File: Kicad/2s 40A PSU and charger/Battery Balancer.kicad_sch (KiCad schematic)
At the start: 18 parts, among them J1 JST XH-S, Q6 Vishay sir404dp, U1 BQ76905RGRR

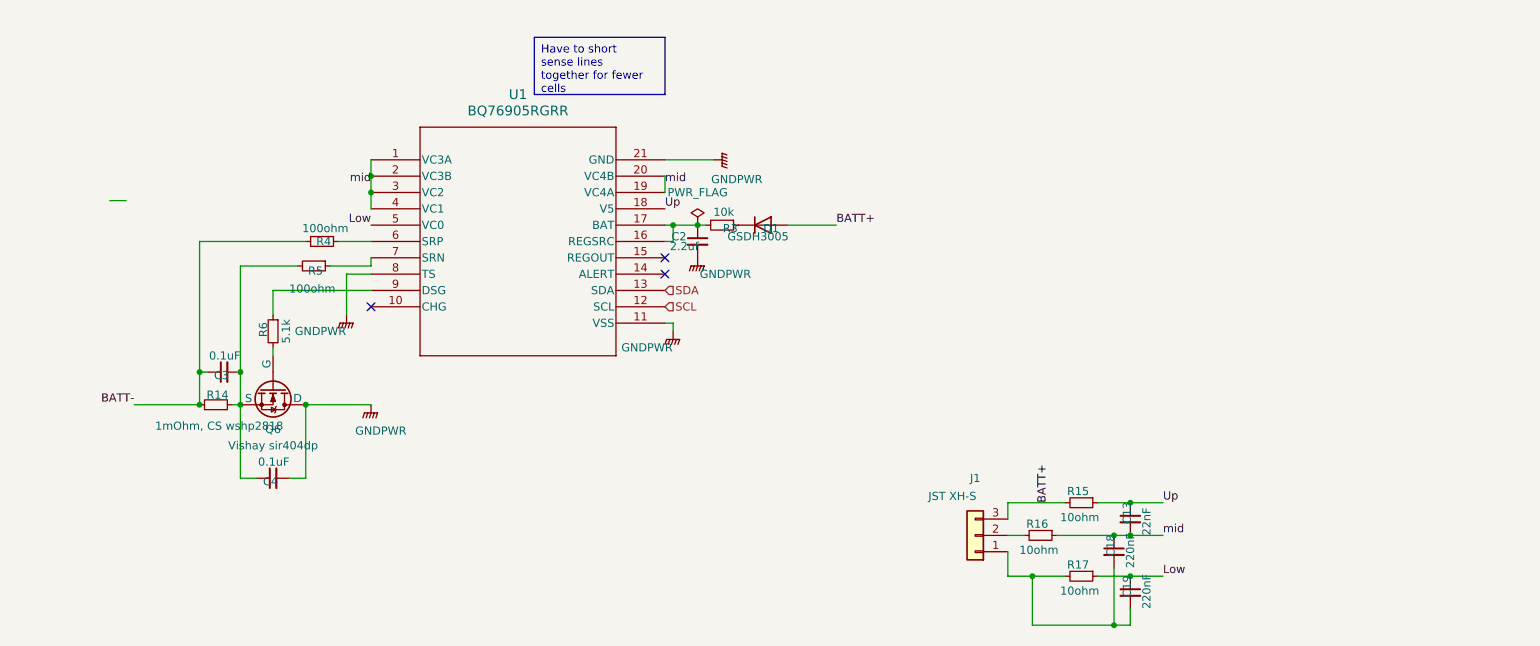
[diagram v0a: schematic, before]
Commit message: Reworked PSU to use CH32X035 and USB-PD
This will save a few bucks and will actually be a cooler solution than just a DC jack connected to some pads
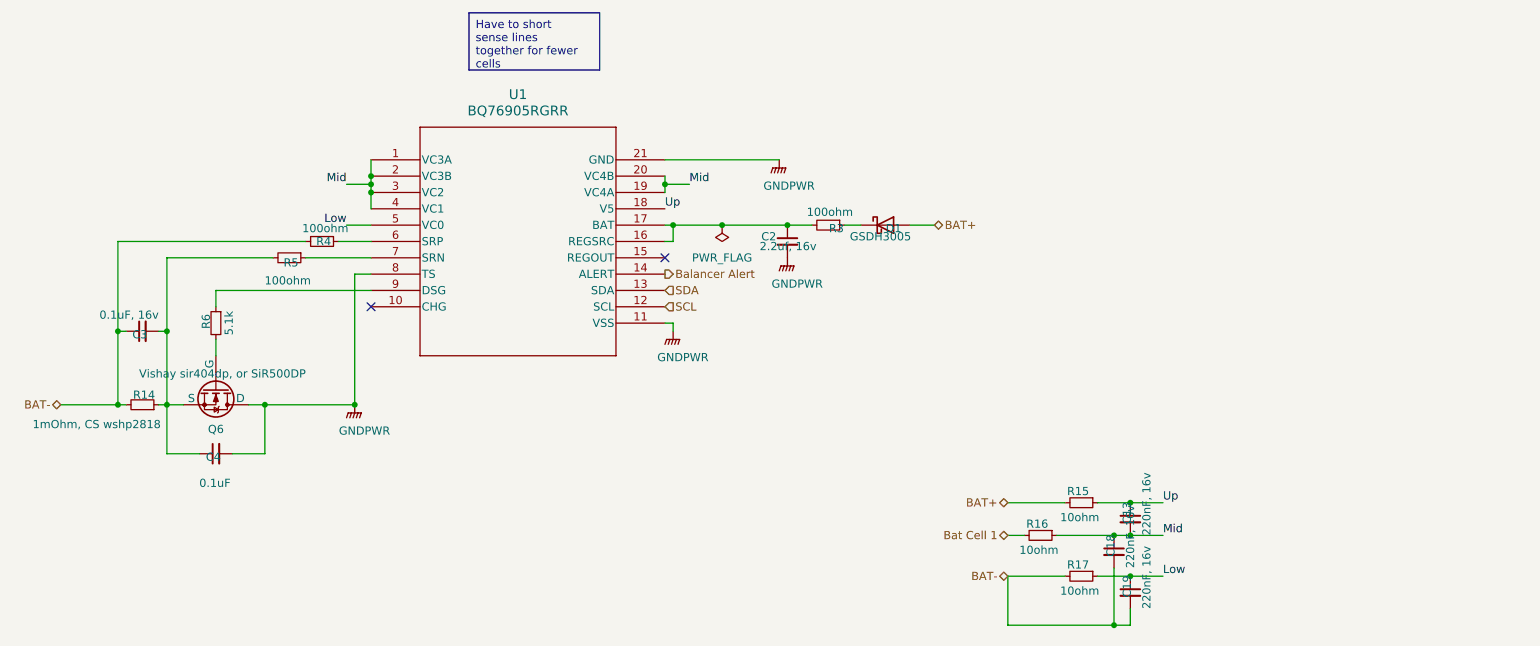
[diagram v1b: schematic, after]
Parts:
- removed J1: JST XH-S, Connector_JST:JST_XH_S3B-XH-A_1x03_P2.50mm_Horizontal, symbol Connector_Generic:Conn_01x03
- C13: value 22nF -> 220nF, 16v; footprint Capacitor_SMD:C_0603_1608Metric -> Capacitor_SMD:C_0402_1005Metric
- C18, C19: value 220nF -> 220nF, 16v; footprint Capacitor_SMD:C_0603_1608Metric -> Capacitor_SMD:C_0402_1005Metric
- C2: value 2.2uf -> 2.2uf, 16v
- C3: value 0.1uF -> 0.1uF, 16v; footprint Capacitor_SMD:C_0603_1608Metric -> Capacitor_SMD:C_0402_1005Metric
- C4: footprint Capacitor_SMD:C_0603_1608Metric -> Capacitor_SMD:C_0402_1005Metric
- D1: symbol Device:D -> Device:D_Schottky
- Q6: value Vishay sir404dp -> Vishay sir404dp, or SiR500DP
- R15, R16, R17, R4, R5, R6: footprint Resistor_SMD:R_0603_1608Metric -> Resistor_SMD:R_0402_1005Metric
- R3: value 10k -> 100ohm; footprint Resistor_SMD:R_0603_1608Metric -> Resistor_SMD:R_0402_1005Metric
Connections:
- net BATT- is gone; now on net BAT-: C3.1, R14.2, R4.2
- net Balancer Alert: now reaches U1.14 (ALERT)
- net Bat Cell 1: now reaches R16.2
- net BAT-: now reaches C18.2, C19.2, R17.2
- net BATT+ renamed BAT+
- net mid renamed Mid
- no-connect marks 3 -> 2
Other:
- moved on the sheet: C2, C3, C4, D1, Q6, R14, R3, R5, R6

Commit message: Improved schematic formatting and visuals
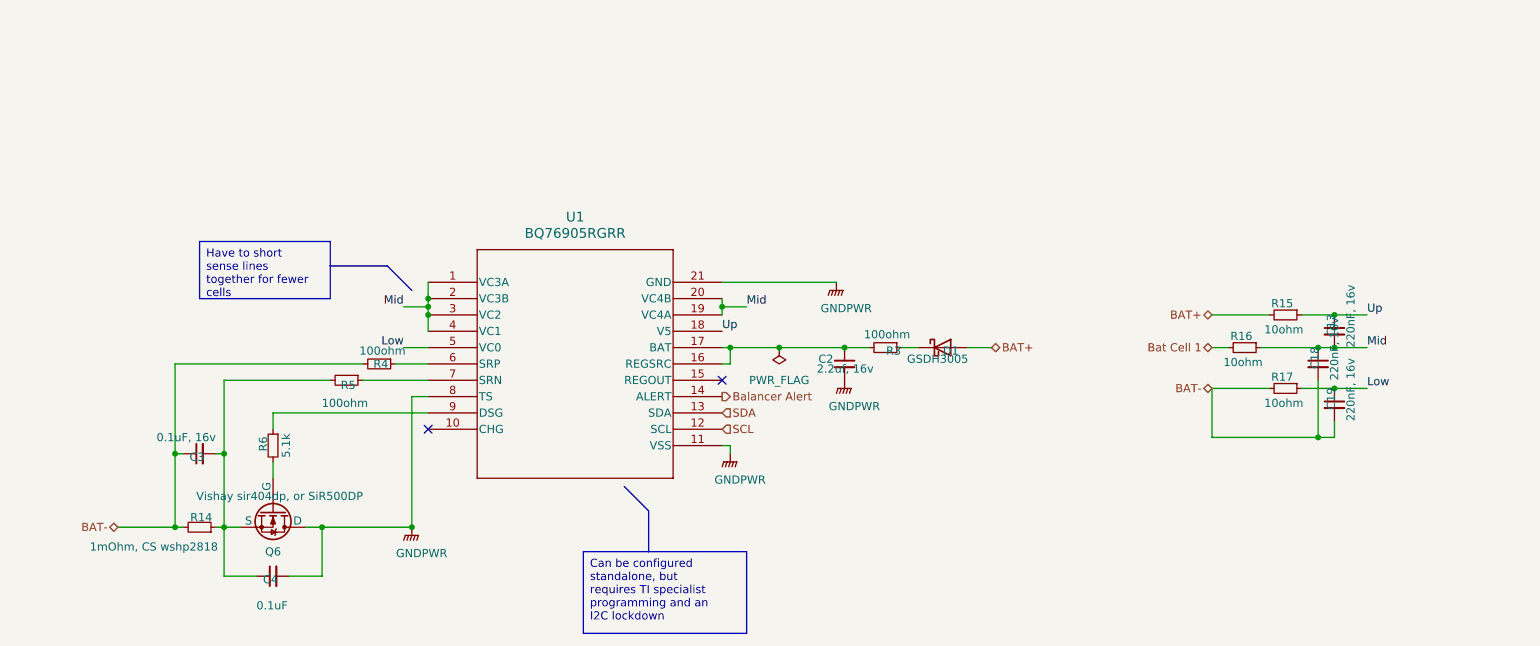
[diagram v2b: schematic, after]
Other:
- moved on the sheet: C13, C18, C19, C2, C3, C4, D1, Q6, R14, R15, R16, R17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

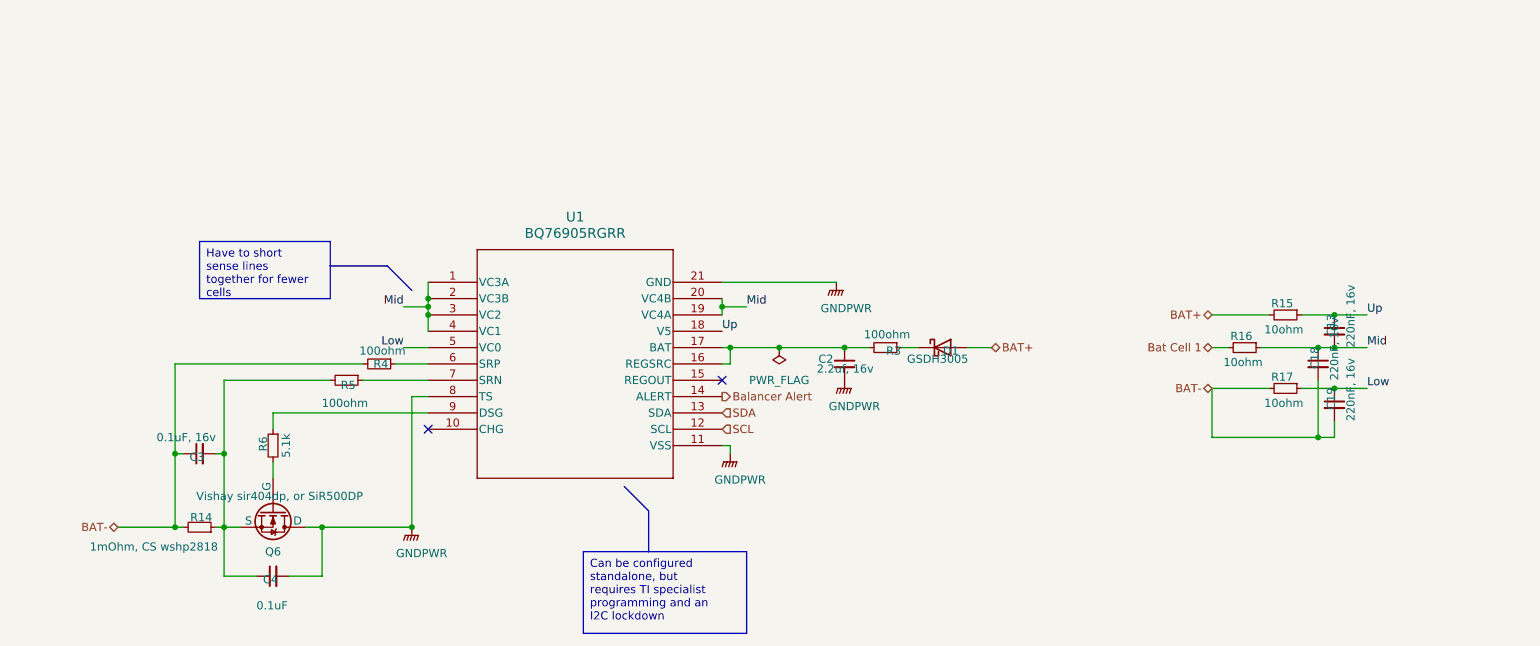
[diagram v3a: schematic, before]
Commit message: Added use of Net Class Directives to speed up routing
I don't have to manually change wire sizes now
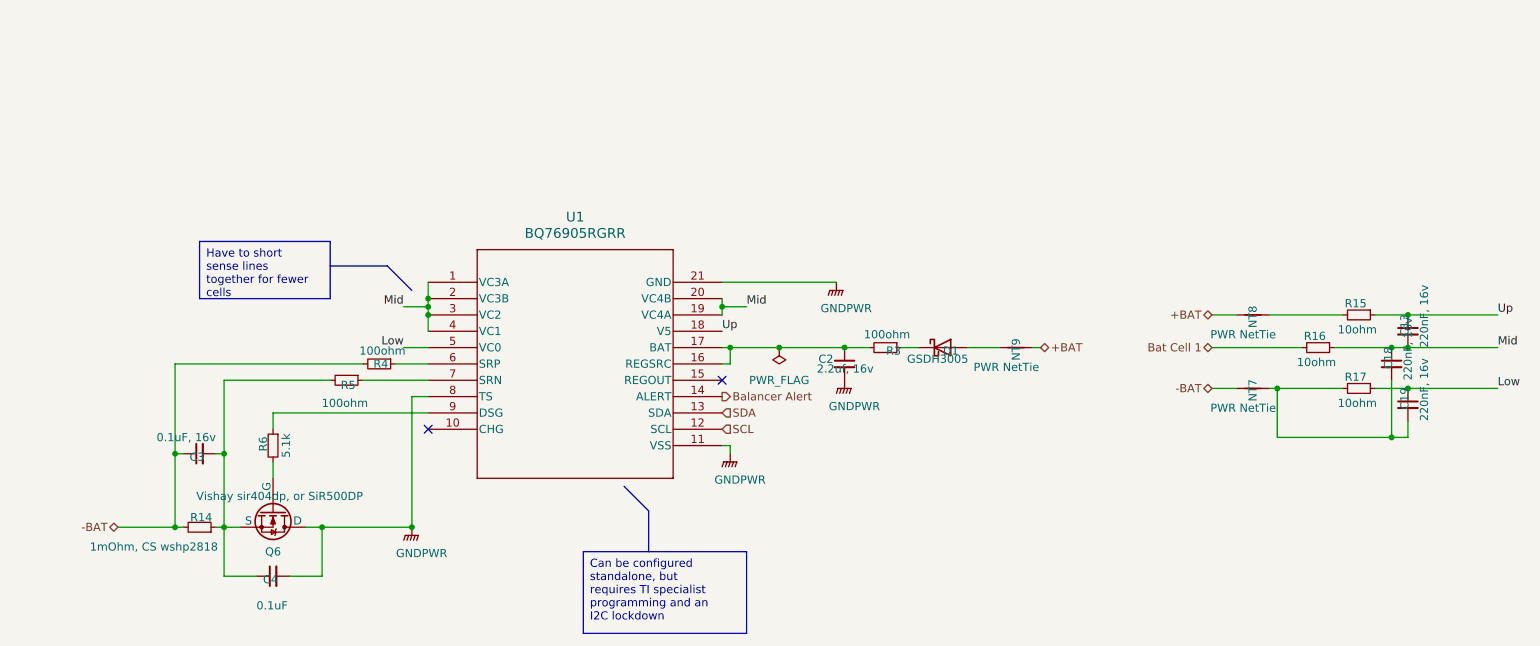
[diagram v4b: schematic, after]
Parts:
- added NT7, NT8, NT9: PWR NetTie, custom_Connector:NetTie-2_SMD_Pad0.28mm, symbol Device:NetTie_2
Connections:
- net BAT+: no longer names the net of D1.2 (A)
- net BAT+: now also NT9.2; no longer R15.2
- net BAT-: no longer names the net of C18.2, C19.2, R17.2
- net BAT-: now also NT7.1; no longer C3.1, R14.2, R4.2
- new net: NT8.1, R15.2
- new net +BAT: NT8.2, NT9.1
- new net -BAT: C3.1, NT7.2, R14.2, R4.2
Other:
- moved on the sheet: C13, C18, C19, R15, R16, R17

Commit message: Updated Sheet Properties
My author name is now in there, and I've added the proper project name.
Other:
- title: (none) -> CACKLE 2s 40A PSU & Charger
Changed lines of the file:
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@@
 	(paper "A4")
 	(title_block
-		(date "2024-11-28")
-		(rev "V1 Alpha")
+		(title "CACKLE 2s 40A PSU & Charger")
+		(date "2024-12-01")
+		(rev "V1")
+		(comment 1 "Author: Asher Edwards")
 	)
 	(junction
